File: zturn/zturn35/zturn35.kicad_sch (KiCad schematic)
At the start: 45 parts, among them Q1 SSM6N15AFU, Q10 SSM6N15AFU, Q11 SSM6N15AFU, Q12 SSM6N15AFU, Q13 SSM6N15AFU, Q14 SSM6N15AFU, Q15 SSM6N15AFU, Q2 SSM6N15AFU, Q3 SSM6N15AFU, Q4 SSM6N15AFU, Q5 SSM6N15AFU, Q6 SSM6N15AFU, Q7 SSM6N15AFU, Q8 SSM6N15AFU, Q9 SSM6N15AFU, U10 74AXP4T245, U11 74AXP4T245, U12 74AXP4T245, U9 74AXP4T245

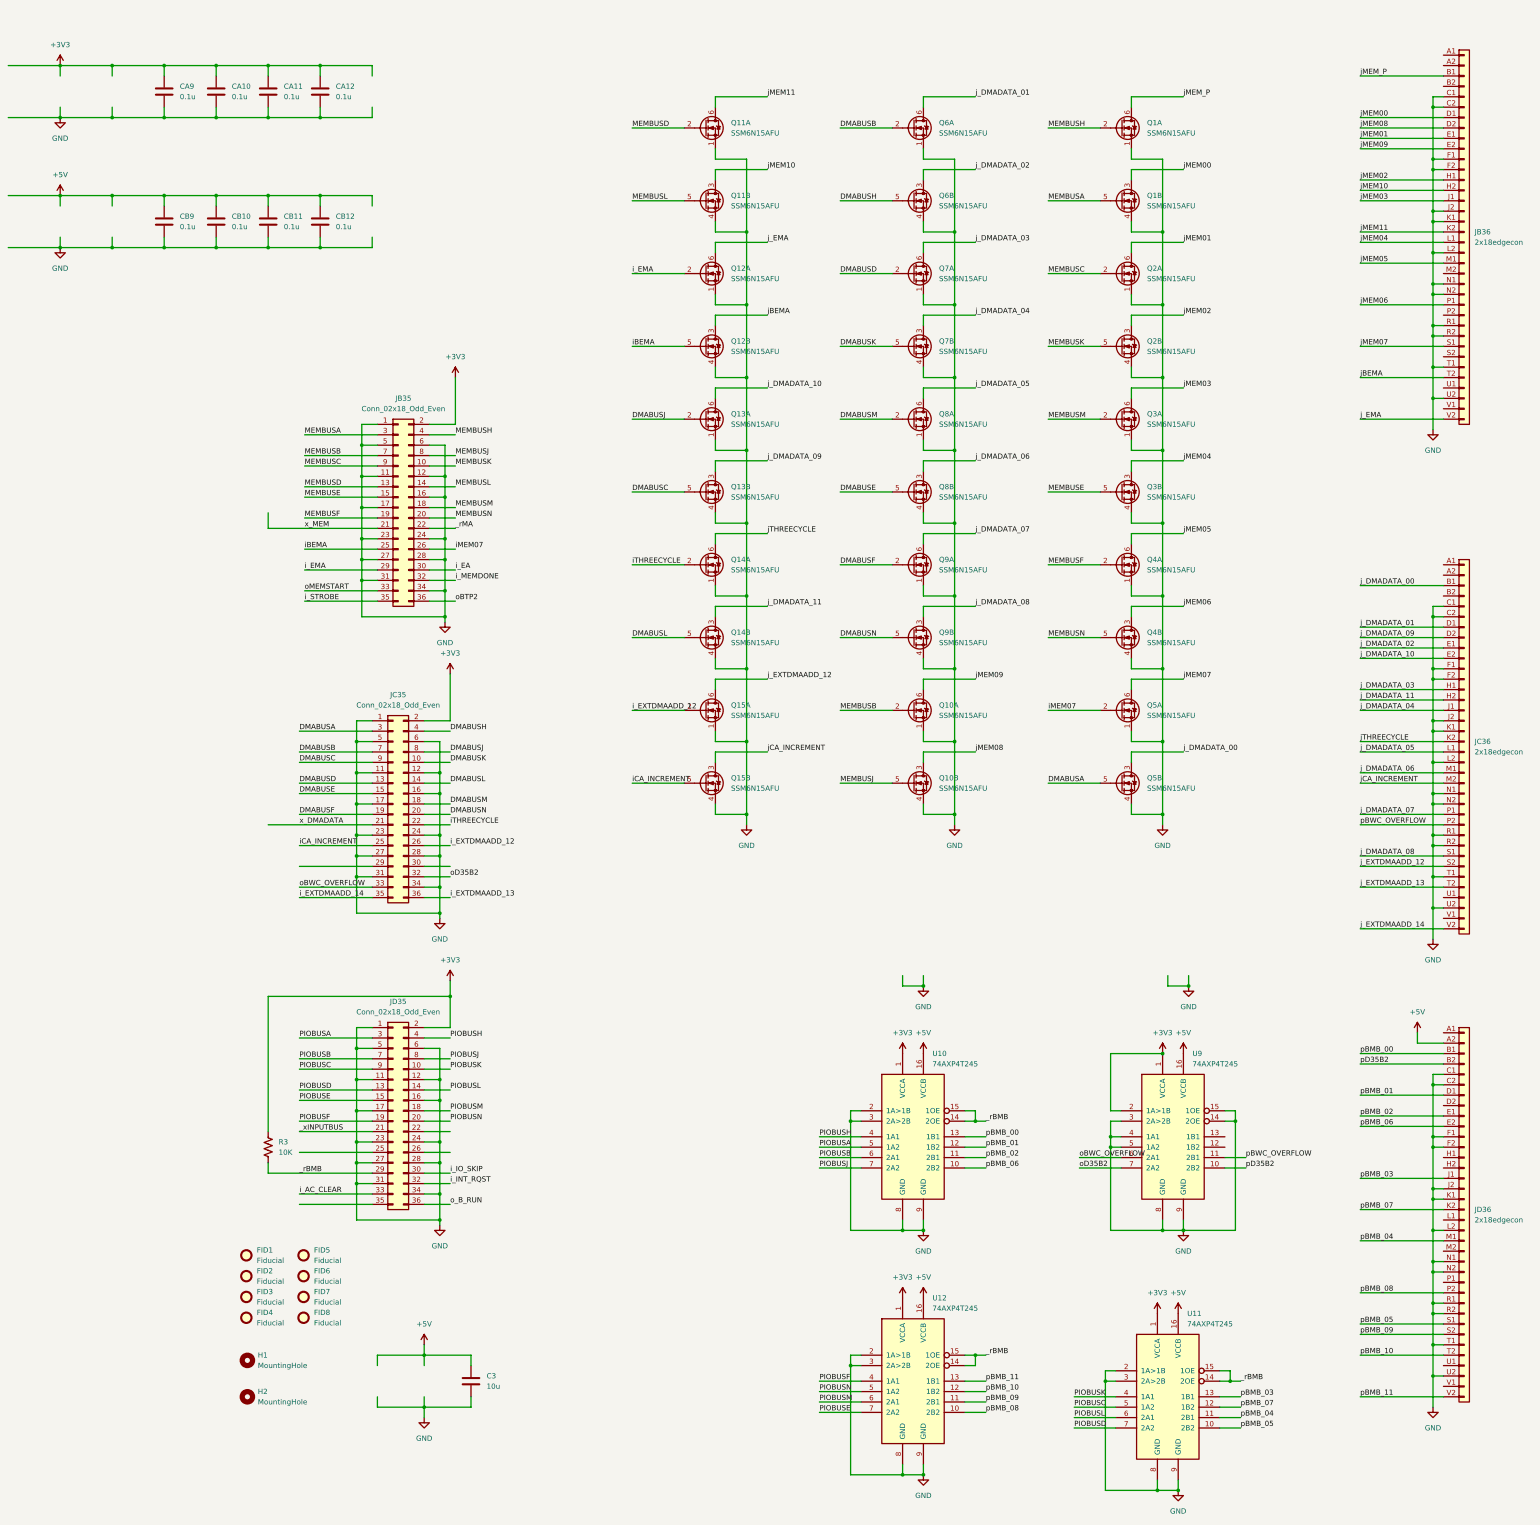
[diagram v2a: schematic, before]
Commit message: update net names on zturn pcbs to match active high/low signal type
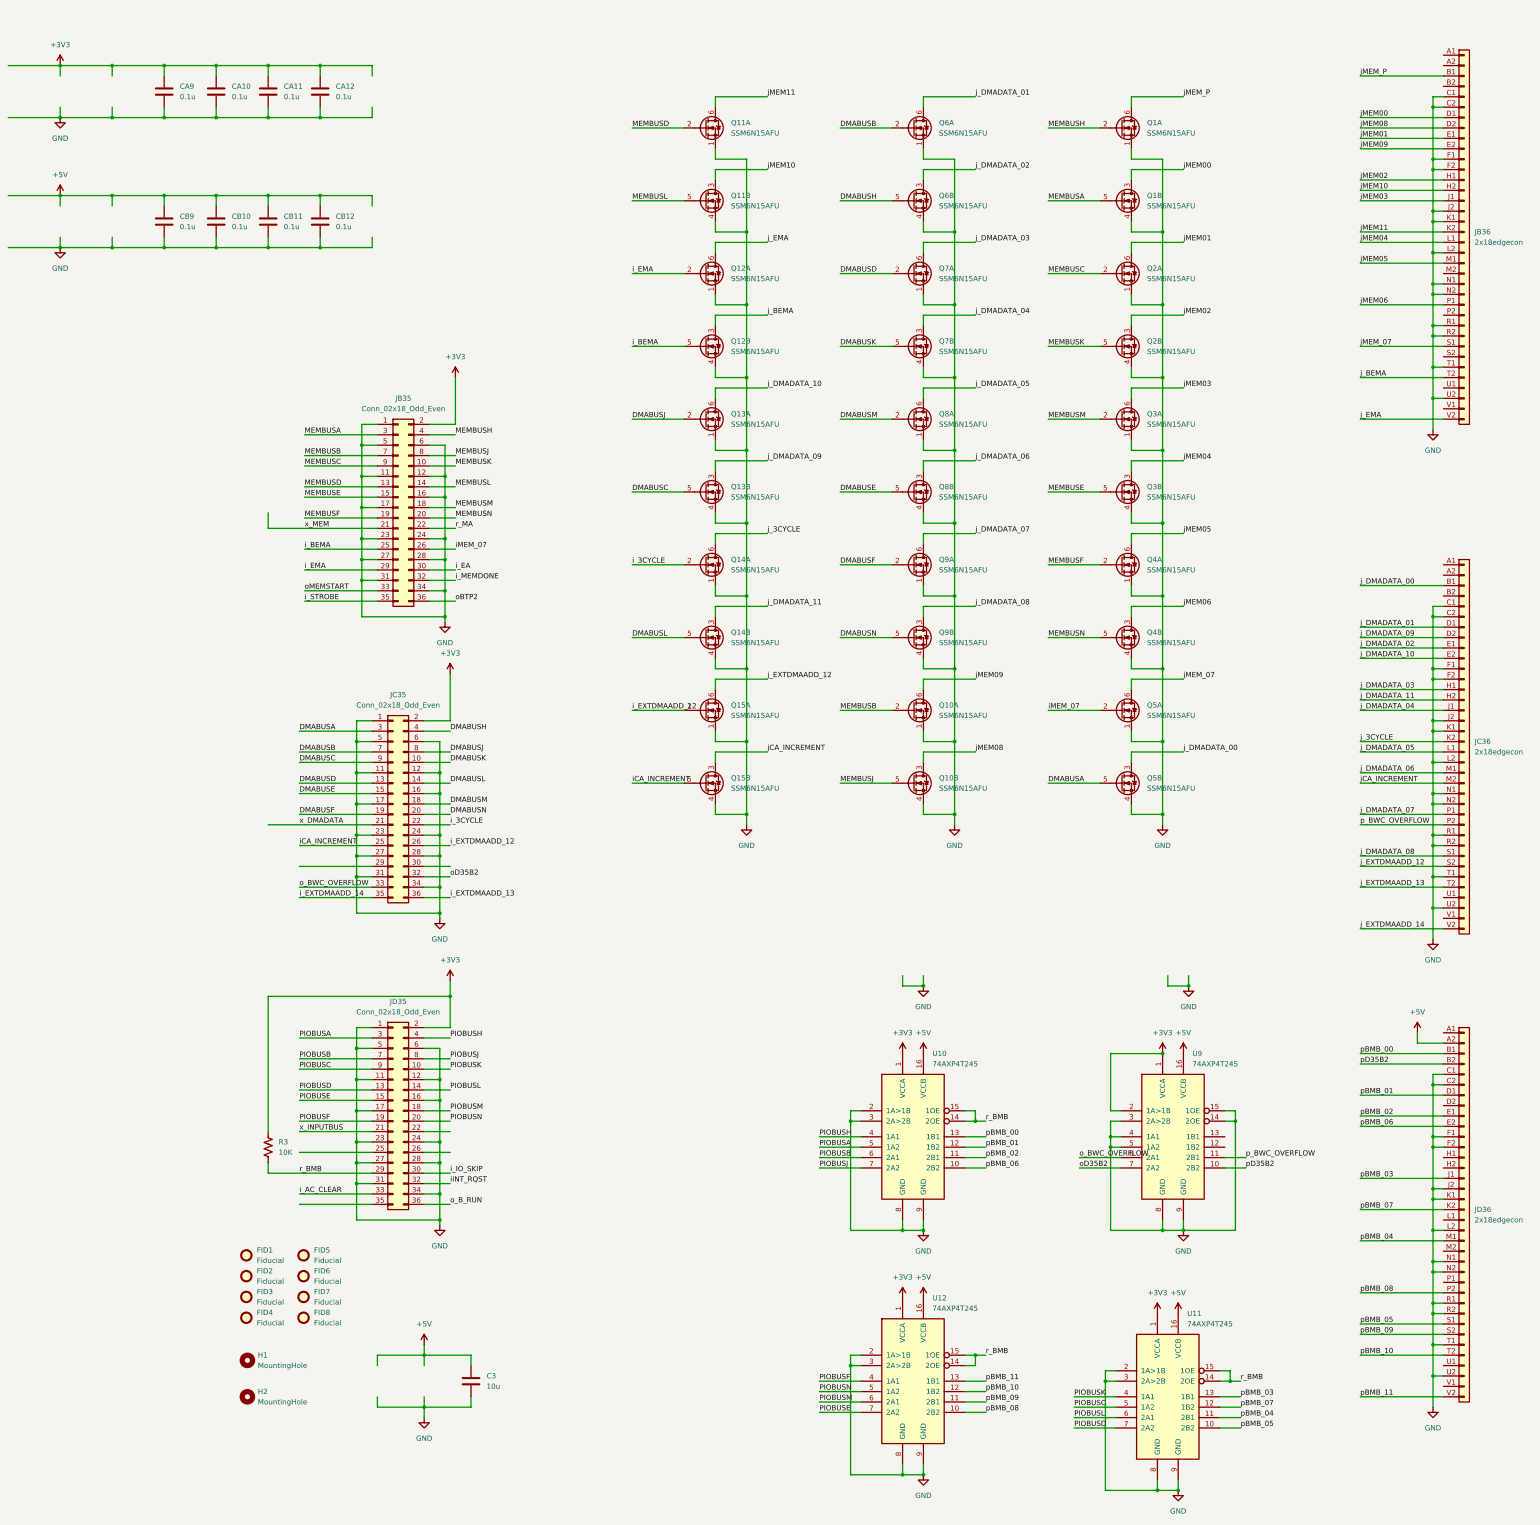
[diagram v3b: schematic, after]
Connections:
- net _rBMB renamed r_BMB
- net _rMA renamed r_MA
- net _xINPUTBUS renamed x_INPUTBUS
- net iBEMA renamed i_BEMA
- net iMEM07 renamed iMEM_07
- net iTHREECYCLE renamed i_3CYCLE
- net i_INT_RQST renamed iINT_RQST
- net jBEMA renamed j_BEMA
- net jMEM07 renamed jMEM_07
- net jTHREECYCLE renamed j_3CYCLE
- net oBWC_OVERFLOW renamed o_BWC_OVERFLOW
- net pBWC_OVERFLOW renamed p_BWC_OVERFLOW
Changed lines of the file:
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@@
     (stroke (width 0) (type default))
   )
-  (label "iMEM07" (at 337.82 143.51 0) (fields_autoplaced)
+  (label "iMEM_07" (at 337.82 143.51 0) (fields_autoplaced)
     (effects (font (size 1.27 1.27)) (justify left bottom))
   )
@@
     (effects (font (size 1.27 1.27)) (justify left bottom))
   )
-  (label "oBWC_OVERFLOW" (at 299.72 226.06 0) (fields_autoplaced)
+  (label "o_BWC_OVERFLOW" (at 299.72 226.06 0) (fields_autoplaced)
     (effects (font (size 1.27 1.27)) (justify left bottom))
   )
@@
     (effects (font (size 1.27 1.27)) (justify left bottom))
   )
-  (label "pBWC_OVERFLOW" (at 530.86 292.1 0) (fields_autoplaced)
+  (label "p_BWC_OVERFLOW" (at 530.86 292.1 0) (fields_autoplaced)
     (effects (font (size 1.27 1.27)) (justify left bottom))
   )
@@
     (effects (font (size 1.27 1.27)) (justify left bottom))
   )
-  (label "iMEM07" (at 482.6 182.88 0) (fields_autoplaced)
+  (label "iMEM_07" (at 482.6 182.88 0) (fields_autoplaced)
     (effects (font (size 1.27 1.27)) (justify left bottom))
   )
@@
     (effects (font (size 1.27 1.27)) (justify left bottom))
   )
-  (label "iBEMA" (at 300.99 143.51 0) (fields_autoplaced)
+  (label "i_BEMA" (at 300.99 143.51 0) (fields_autoplaced)
     (effects (font (size 1.27 1.27)) (justify left bottom))
   )
@@
     (effects (font (size 1.27 1.27)) (justify left bottom))
   )
-  (label "_rBMB" (at 529.59 346.71 0) (fields_autoplaced)
+  (label "r_BMB" (at 529.59 346.71 0) (fields_autoplaced)
     (effects (font (size 1.27 1.27)) (justify left bottom))
   )
@@
     (effects (font (size 1.27 1.27)) (justify left bottom))
   )
-  (label "_rBMB" (at 467.36 283.21 0) (fields_autoplaced)
+  (label "r_BMB" (at 467.36 283.21 0) (fields_autoplaced)
     (effects (font (size 1.27 1.27)) (justify left bottom))
   )
@@
     (effects (font (size 1.27 1.27)) (justify left bottom))
   )
-  (label "jMEM07" (at 515.62 175.26 0) (fields_autoplaced)
+  (label "jMEM_07" (at 515.62 175.26 0) (fields_autoplaced)
     (effects (font (size 1.27 1.27)) (justify left bottom))
   )
@@
     (effects (font (size 1.27 1.27)) (justify left bottom))
   )
-  (label "iTHREECYCLE" (at 336.55 210.82 0) (fields_autoplaced)
+  (label "i_3CYCLE" (at 336.55 210.82 0) (fields_autoplaced)
     (effects (font (size 1.27 1.27)) (justify left bottom))
   )
@@
     (effects (font (size 1.27 1.27)) (justify left bottom))
   )
-  (label "oBWC_OVERFLOW" (at 490.22 292.1 0) (fields_autoplaced)
+  (label "o_BWC_OVERFLOW" (at 490.22 292.1 0) (fields_autoplaced)
     (effects (font (size 1.27 1.27)) (justify left bottom))
   )
@@
     (effects (font (size 1.27 1.27)) (justify left bottom))
   )
-  (label "i_INT_RQST" (at 336.55 298.45 0) (fields_autoplaced)
+  (label "iINT_RQST" (at 336.55 298.45 0) (fields_autoplaced)
     (effects (font (size 1.27 1.27)) (justify left bottom))
   )
@@
     (effects (font (size 1.27 1.27)) (justify left bottom))
   )
-  (label "pBWC_OVERFLOW" (at 558.8 210.82 0) (fields_autoplaced)
+  (label "p_BWC_OVERFLOW" (at 558.8 210.82 0) (fields_autoplaced)
     (effects (font (size 1.27 1.27)) (justify left bottom))
   )
@@
     (effects (font (size 1.27 1.27)) (justify left bottom))
   )
-  (label "jTHREECYCLE" (at 414.02 139.7 0) (fields_autoplaced)
+  (label "j_3CYCLE" (at 414.02 139.7 0) (fields_autoplaced)
     (effects (font (size 1.27 1.27)) (justify left bottom))
   )
@@
     (effects (font (size 1.27 1.27)) (justify left bottom))
   )
-  (label "jMEM07" (at 558.8 93.98 0) (fields_autoplaced)
+  (label "jMEM_07" (at 558.8 93.98 0) (fields_autoplaced)
     (effects (font (size 1.27 1.27)) (justify left bottom))
   )
@@
     (effects (font (size 1.27 1.27)) (justify left bottom))
   )
-  (label "iBEMA" (at 381 93.98 0) (fields_autoplaced)
+  (label "i_BEMA" (at 381 93.98 0) (fields_autoplaced)
     (effects (font (size 1.27 1.27)) (justify left bottom))
   )
@@
     (effects (font (size 1.27 1.27)) (justify left bottom))
   )
-  (label "_xINPUTBUS" (at 299.72 285.75 0) (fields_autoplaced)
+  (label "x_INPUTBUS" (at 299.72 285.75 0) (fields_autoplaced)
     (effects (font (size 1.27 1.27)) (justify left bottom))
   )
@@
     (effects (font (size 1.27 1.27)) (justify left bottom))
   )
-  (label "_rBMB" (at 467.36 340.36 0) (fields_autoplaced)
+  (label "r_BMB" (at 467.36 340.36 0) (fields_autoplaced)
     (effects (font (size 1.27 1.27)) (justify left bottom))
   )
@@
     (effects (font (size 1.27 1.27)) (justify left bottom))
   )
-  (label "iTHREECYCLE" (at 381 147.32 0) (fields_autoplaced)
+  (label "i_3CYCLE" (at 381 147.32 0) (fields_autoplaced)
     (effects (font (size 1.27 1.27)) (justify left bottom))
   )
@@
     (effects (font (size 1.27 1.27)) (justify left bottom))
   )
-  (label "_rMA" (at 337.82 138.43 0) (fields_autoplaced)
+  (label "r_MA" (at 337.82 138.43 0) (fields_autoplaced)
     (effects (font (size 1.27 1.27)) (justify left bottom))
   )
@@
     (effects (font (size 1.27 1.27)) (justify left bottom))
   )
-  (label "_rBMB" (at 299.72 295.91 0) (fields_autoplaced)
+  (label "r_BMB" (at 299.72 295.91 0) (fields_autoplaced)
     (effects (font (size 1.27 1.27)) (justify left bottom))
   )
@@
     (effects (font (size 1.27 1.27)) (justify left bottom))
   )
-  (label "jBEMA" (at 414.02 86.36 0) (fields_autoplaced)
+  (label "j_BEMA" (at 414.02 86.36 0) (fields_autoplaced)
     (effects (font (size 1.27 1.27)) (justify left bottom))
   )
@@
     (effects (font (size 1.27 1.27)) (justify left bottom))
   )
-  (label "jTHREECYCLE" (at 558.8 190.5 0) (fields_autoplaced)
+  (label "j_3CYCLE" (at 558.8 190.5 0) (fields_autoplaced)
     (effects (font (size 1.27 1.27)) (justify left bottom))
   )
@@
     (effects (font (size 1.27 1.27)) (justify left bottom))
   )
-  (label "jBEMA" (at 558.8 101.6 0) (fields_autoplaced)
-    (effects (font (size 1.27 1.27)) (justify left bottom))
-  )
+  (label "j_BEMA" (at 558.8 101.6 0) (fields_autoplaced)
+    (effects (font (size 1.27 1.27)) (justify left bottom))
+  )

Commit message: update software and further updates to firmware/pcbs
...for invertering transistors

./z8lsimtest works
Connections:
- net iCA_INCREMENT renamed i_CA_INCRMNT
- net iMEM_07 renamed i_MEM_07
- net i_3CYCLE renamed i3CYCLE
- net i_AC_CLEAR renamed iAC_CLEAR
- net i_BEMA renamed iBEMA
- net i_EMA renamed iEMA
- net i_EXTDMAADD_12 renamed iEXTDMAADD_12
- net i_IO_SKIP renamed iIO_SKIP
- net jCA_INCREMENT renamed jCA_INCRMNT
- net o_B_RUN renamed oB_RUN
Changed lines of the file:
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@@
     (stroke (width 0) (type default))
   )
-  (label "iMEM_07" (at 337.82 143.51 0) (fields_autoplaced)
+  (label "i_MEM_07" (at 337.82 143.51 0) (fields_autoplaced)
     (effects (font (size 1.27 1.27)) (justify left bottom))
   )
@@
     (effects (font (size 1.27 1.27)) (justify left bottom))
   )
-  (label "iMEM_07" (at 482.6 182.88 0) (fields_autoplaced)
+  (label "i_MEM_07" (at 482.6 182.88 0) (fields_autoplaced)
     (effects (font (size 1.27 1.27)) (justify left bottom))
   )
@@
     (effects (font (size 1.27 1.27)) (justify left bottom))
   )
-  (label "i_BEMA" (at 300.99 143.51 0) (fields_autoplaced)
+  (label "iBEMA" (at 300.99 143.51 0) (fields_autoplaced)
     (effects (font (size 1.27 1.27)) (justify left bottom))
   )
@@
     (effects (font (size 1.27 1.27)) (justify left bottom))
   )
-  (label "i_EMA" (at 381 76.2 0) (fields_autoplaced)
+  (label "iEMA" (at 381 76.2 0) (fields_autoplaced)
     (effects (font (size 1.27 1.27)) (justify left bottom))
   )
@@
     (effects (font (size 1.27 1.27)) (justify left bottom))
   )
-  (label "i_IO_SKIP" (at 336.55 295.91 0) (fields_autoplaced)
+  (label "iIO_SKIP" (at 336.55 295.91 0) (fields_autoplaced)
     (effects (font (size 1.27 1.27)) (justify left bottom))
   )
@@
     (effects (font (size 1.27 1.27)) (justify left bottom))
   )
-  (label "i_3CYCLE" (at 336.55 210.82 0) (fields_autoplaced)
+  (label "i3CYCLE" (at 336.55 210.82 0) (fields_autoplaced)
     (effects (font (size 1.27 1.27)) (justify left bottom))
   )
@@
     (effects (font (size 1.27 1.27)) (justify left bottom))
   )
-  (label "jCA_INCREMENT" (at 414.02 193.04 0) (fields_autoplaced)
+  (label "jCA_INCRMNT" (at 414.02 193.04 0) (fields_autoplaced)
     (effects (font (size 1.27 1.27)) (justify left bottom))
   )
@@
     (effects (font (size 1.27 1.27)) (justify left bottom))
   )
-  (label "i_EMA" (at 300.99 148.59 0) (fields_autoplaced)
+  (label "iEMA" (at 300.99 148.59 0) (fields_autoplaced)
     (effects (font (size 1.27 1.27)) (justify left bottom))
   )
@@
     (effects (font (size 1.27 1.27)) (justify left bottom))
   )
-  (label "iCA_INCREMENT" (at 299.72 215.9 0) (fields_autoplaced)
+  (label "i_CA_INCRMNT" (at 299.72 215.9 0) (fields_autoplaced)
     (effects (font (size 1.27 1.27)) (justify left bottom))
   )
@@
     (effects (font (size 1.27 1.27)) (justify left bottom))
   )
-  (label "i_EXTDMAADD_12" (at 336.55 215.9 0) (fields_autoplaced)
+  (label "iEXTDMAADD_12" (at 336.55 215.9 0) (fields_autoplaced)
     (effects (font (size 1.27 1.27)) (justify left bottom))
   )
@@
     (effects (font (size 1.27 1.27)) (justify left bottom))
   )
-  (label "i_EXTDMAADD_12" (at 381 182.88 0) (fields_autoplaced)
+  (label "iEXTDMAADD_12" (at 381 182.88 0) (fields_autoplaced)
     (effects (font (size 1.27 1.27)) (justify left bottom))
   )
@@
     (effects (font (size 1.27 1.27)) (justify left bottom))
   )
-  (label "i_BEMA" (at 381 93.98 0) (fields_autoplaced)
+  (label "iBEMA" (at 381 93.98 0) (fields_autoplaced)
     (effects (font (size 1.27 1.27)) (justify left bottom))
   )
@@
     (effects (font (size 1.27 1.27)) (justify left bottom))
   )
-  (label "o_B_RUN" (at 336.55 303.53 0) (fields_autoplaced)
+  (label "oB_RUN" (at 336.55 303.53 0) (fields_autoplaced)
     (effects (font (size 1.27 1.27)) (justify left bottom))
   )
@@
     (effects (font (size 1.27 1.27)) (justify left bottom))
   )
-  (label "i_3CYCLE" (at 381 147.32 0) (fields_autoplaced)
+  (label "i3CYCLE" (at 381 147.32 0) (fields_autoplaced)
     (effects (font (size 1.27 1.27)) (justify left bottom))
   )
@@
     (effects (font (size 1.27 1.27)) (justify left bottom))
   )
-  (label "i_AC_CLEAR" (at 299.72 300.99 0) (fields_autoplaced)
+  (label "iAC_CLEAR" (at 299.72 300.99 0) (fields_autoplaced)
     (effects (font (size 1.27 1.27)) (justify left bottom))
   )
@@
     (effects (font (size 1.27 1.27)) (justify left bottom))
   )
-  (label "iCA_INCREMENT" (at 381 200.66 0) (fields_autoplaced)
+  (label "i_CA_INCRMNT" (at 381 200.66 0) (fields_autoplaced)
     (effects (font (size 1.27 1.27)) (justify left bottom))
   )
@@
     (effects (font (size 1.27 1.27)) (justify left bottom))
   )
-  (label "jCA_INCREMENT" (at 558.8 200.66 0) (fields_autoplaced)
-    (effects (font (size 1.27 1.27)) (justify left bottom))
-  )
+  (label "jCA_INCRMNT" (at 558.8 200.66 0) (fields_autoplaced)
+    (effects (font (size 1.27 1.27)) (justify left bottom))
+  )
